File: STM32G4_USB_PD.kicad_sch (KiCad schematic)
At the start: 22 parts, among them J1 USB4105-GF-A, J2 8.06.16_J-LINK_6-PIN_NEEDLE_A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, J3 Conn_01x04, J4 Conn_01x02, Q1 2N7002K, U1 STM32G431C8T6, U2 AP2205-W5-7

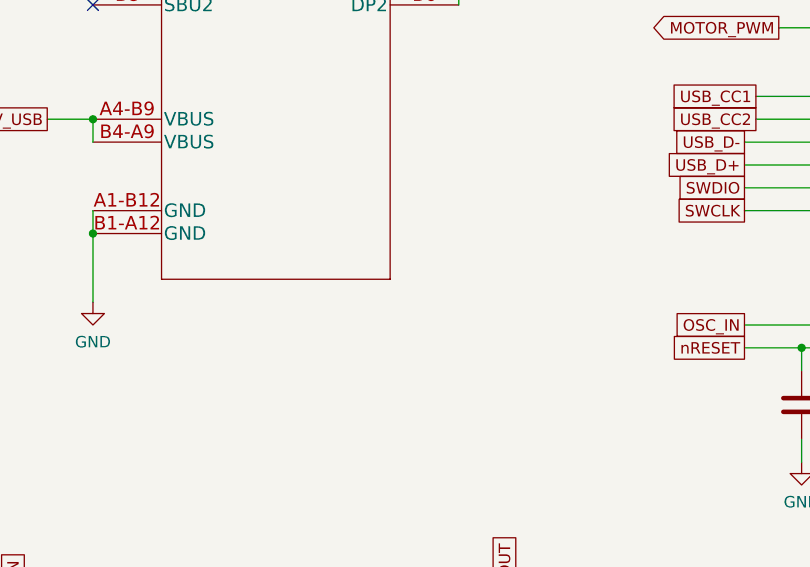
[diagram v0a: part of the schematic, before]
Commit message: improve VBUS trace width
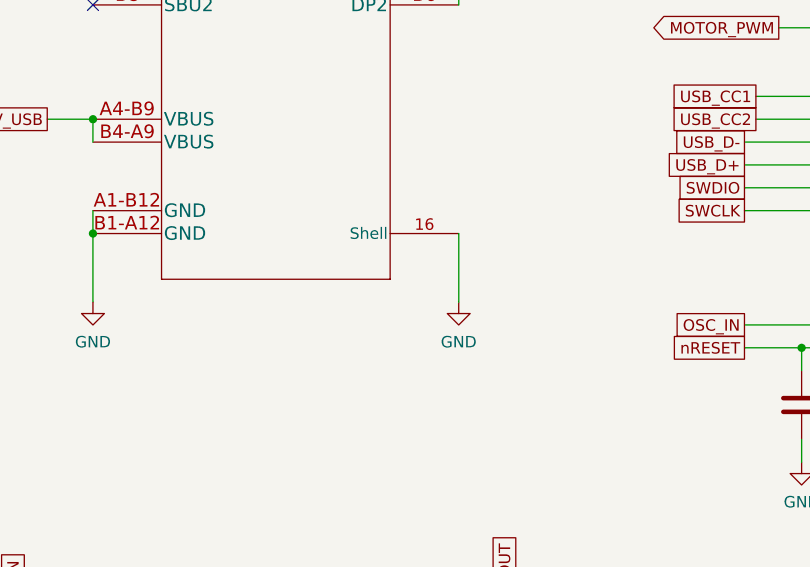
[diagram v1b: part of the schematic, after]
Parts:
- J1: symbol USB4105-GF-A:USB4105-GF-A -> Anh_Nguyen:USB4105-GF-A
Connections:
- net GND: now also J1.13 (Shell), J1.14 (Shell), J1.15 (Shell), J1.16 (Shell)
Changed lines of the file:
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@@
+    (stroke (width 0) (type default) (color 0 0 0 0))
+  )
+  (wire (pts (xy 69.85 64.77) (xy 69.85 72.39))
     (stroke (width 0) (type default) (color 0 0 0 0))
   )
@@
     (pin "6")
   )
-  (symbol (lib_id "USB4105-GF-A:USB4105-GF-A") (at 29.21 29.21 0) (unit 1)
+  (symbol (lib_id "Anh_Nguyen:USB4105-GF-A") (at 29.21 29.21 0) (unit 1)
     (in_bom yes) (on_board yes) (fields_autoplaced)
     (property "Reference" "J1" (id 0) (at 49.53 17.4424 0)
@@
       (effects (font (size 1.524 1.524)))
     )
+    (pin "13")
+    (pin "14")
+    (pin "15")
+    (pin "16")
     (pin "A1-B12")
     (pin "A4-B9")
@@
     (pin "1")
     (pin "2")
+  )
+  (symbol (lib_id "power:GND") (at 69.85 72.39 0) (unit 1)
+    (in_bom yes) (on_board yes) (fields_autoplaced)
+    (property "Reference" "#PWR?" (id 0) (at 69.85 78.74 0)
+      (effects (font (size 1.27 1.27)) hide)
+    )
+    (property "Value" "GND" (id 1) (at 69.85 76.8334 0))
+    (property "Footprint" "" (id 2) (at 69.85 72.39 0)
+      (effects (font (size 1.27 1.27)) hide)
+    )
+    (property "Datasheet" "" (id 3) (at 69.85 72.39 0)
+      (effects (font (size 1.27 1.27)) hide)
+    )
+    (pin "1")
   )
   (symbol (lib_id "power:+3.3V") (at 154.94 154.94 0) (unit 1)
@@
       (reference "#PWR016") (unit 1) (value "GND") (footprint "")
     )
+    (path "/a4f7b292-24dc-4c85-ab4a-763bfb7782b5"
+      (reference "#PWR?") (unit 1) (value "GND") (footprint "")
+    )
     (path "/fda9325a-afce-4a4f-a3af-14a7f5999ce8"

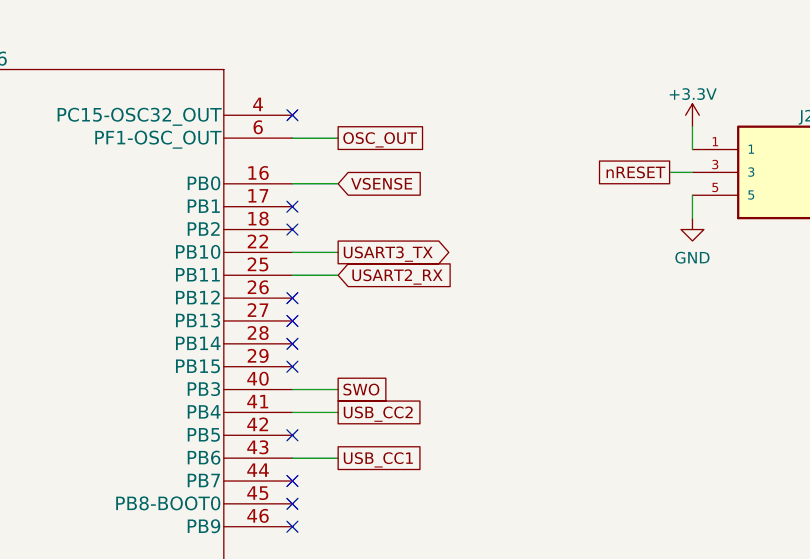
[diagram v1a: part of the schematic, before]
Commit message: add usb-C, USB Device and PWM firmware
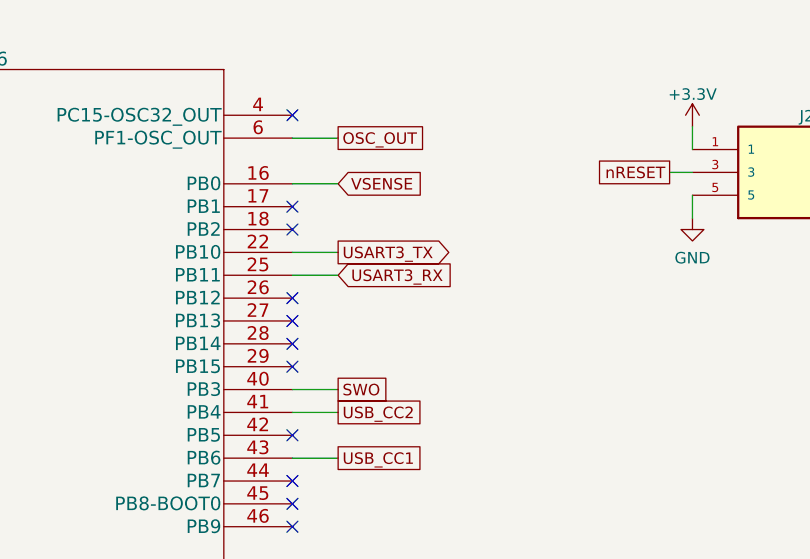
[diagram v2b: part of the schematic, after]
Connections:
- net USART2_RX: no longer U1.25 (PB11)
- new net USART3_RX: U1.25 (PB11)
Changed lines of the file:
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@@
     )
   )
-  (global_label "USART2_RX" (shape input) (at 196.85 41.91 0) (fields_autoplaced)
+  (global_label "USART3_RX" (shape input) (at 196.85 41.91 0) (fields_autoplaced)
     (effects (font (size 1.27 1.27)) (justify left))
-    (property "Intersheet References" "${INTERSHEET_REFS}" (id 0) (at 209.786 41.9894 0)
+    (property "Intersheet References" "${INTERSHEET_REFS}" (id 0) (at 209.786 41.8306 0)
       (effects (font (size 1.27 1.27)) (justify left) hide)
     )
